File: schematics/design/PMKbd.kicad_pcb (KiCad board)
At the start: 2 copper layers, 28.1 x 39.6 mm, 92 parts, among them J1 Conn_01x01, J10 Conn_01x01, J11 Conn_01x01, J12 Conn_01x01, J13 Conn_01x01, J14 Conn_01x01, J15 Conn_01x01, J16 Conn_01x01, J17 Conn_01x01, J18 Conn_01x01, J19 Conn_01x01, J2 Conn_01x01, J20 Conn_01x01, J21 Conn_01x01, J22 Conn_01x01, J23 Conn_01x01, J24 Conn_01x01, J25 Conn_01x01, J26 Conn_01x01, J27 Conn_01x01, J28 Conn_01x01, J29 Conn_01x01, J3 Conn_01x01, J30 Conn_01x01, J31 Conn_01x01, J32 Conn_01x01, J33 Conn_01x01, J34 Conn_01x01, J35 Conn_01x01, J36 Conn_01x01, J37 Conn_01x01, J38 Conn_01x01, J39 Conn_01x01, J4 Conn_01x01, J40 Conn_01x01, J41 Conn_01x01, J42 Conn_01x01, J43 Conn_01x01, J44 Conn_01x01, J45 Conn_01x01, J46 Conn_01x01, J47 Conn_01x01, J48 Conn_01x01, J49 Conn_01x01, J5 Conn_01x01, J50 Conn_01x01, J51 Conn_01x01, J52 Conn_01x01, J53 Conn_01x01, J54 Conn_01x01, J55 Conn_01x01, J56 Conn_01x01, J57 Conn_01x01, J58 Conn_01x01, J59 Conn_01x01, J6 Conn_01x01, J60 Conn_01x01, J61 Conn_01x01, J62 Conn_01x01, J63 Conn_01x01, J64 Conn_01x01, J65 Conn_01x01, J66 Conn_01x01, J67 Conn_01x01, J68 Conn_01x01, J69 Conn_01x01, J7 Conn_01x01, J70 Conn_01x01, J71 Conn_01x01, J72 Conn_01x01, J73 Conn_01x01, J74 Conn_01x01, J8 Conn_01x01, J9 Conn_01x01, Q1 2N2222, Q2 2N2222, U1 Core51822_(B), U2 LT1117-3.3, U3 MCP73831-2-OT, U4 Core51822_(B)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

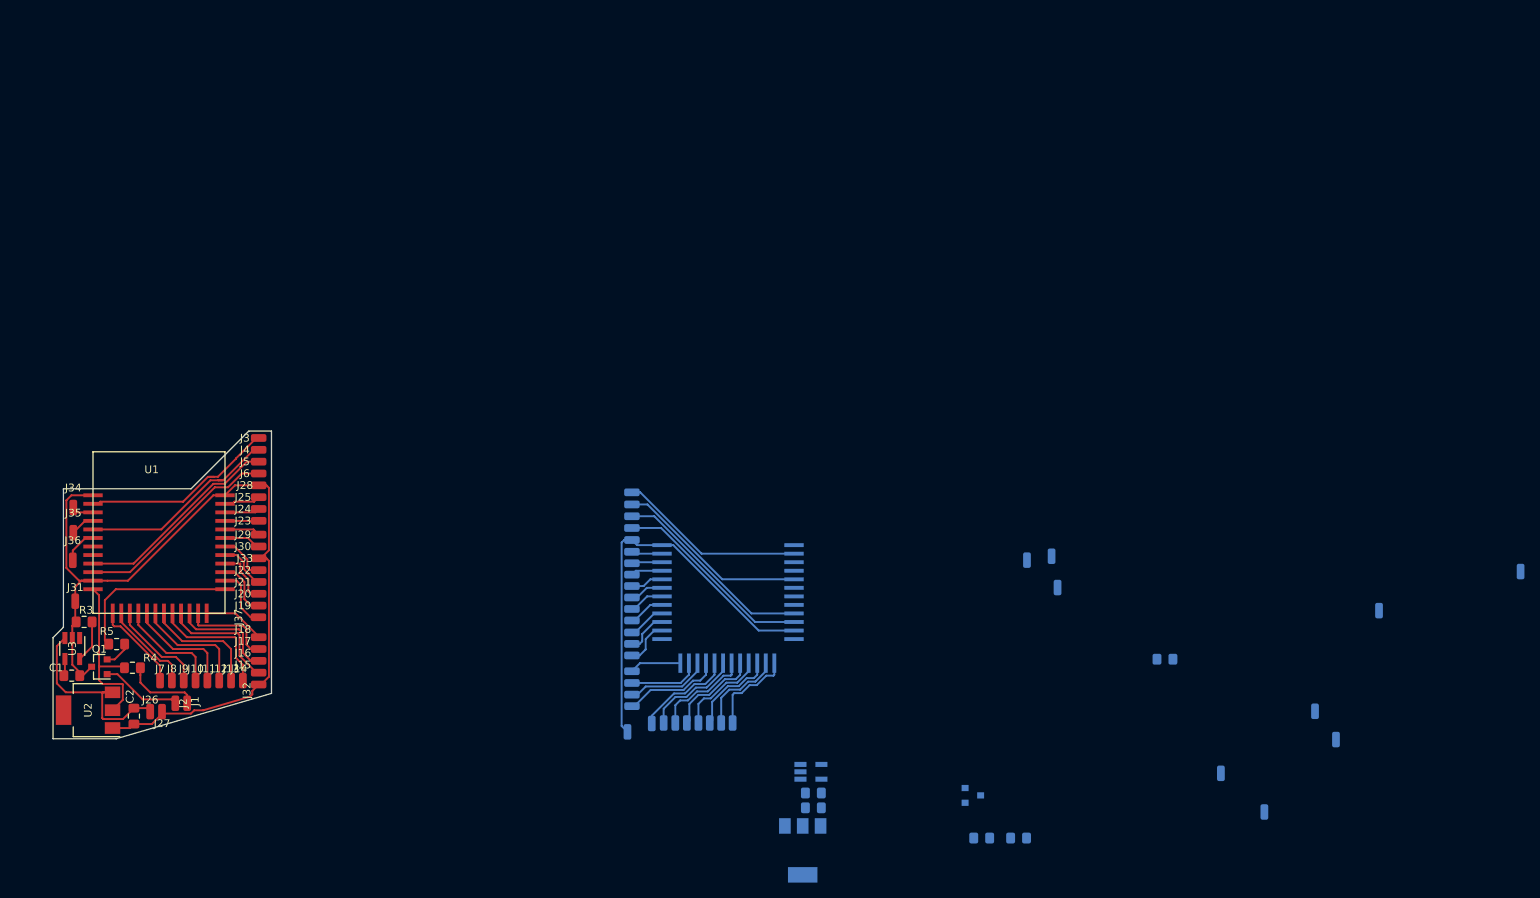
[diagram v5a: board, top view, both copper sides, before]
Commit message: first time right and left layouted
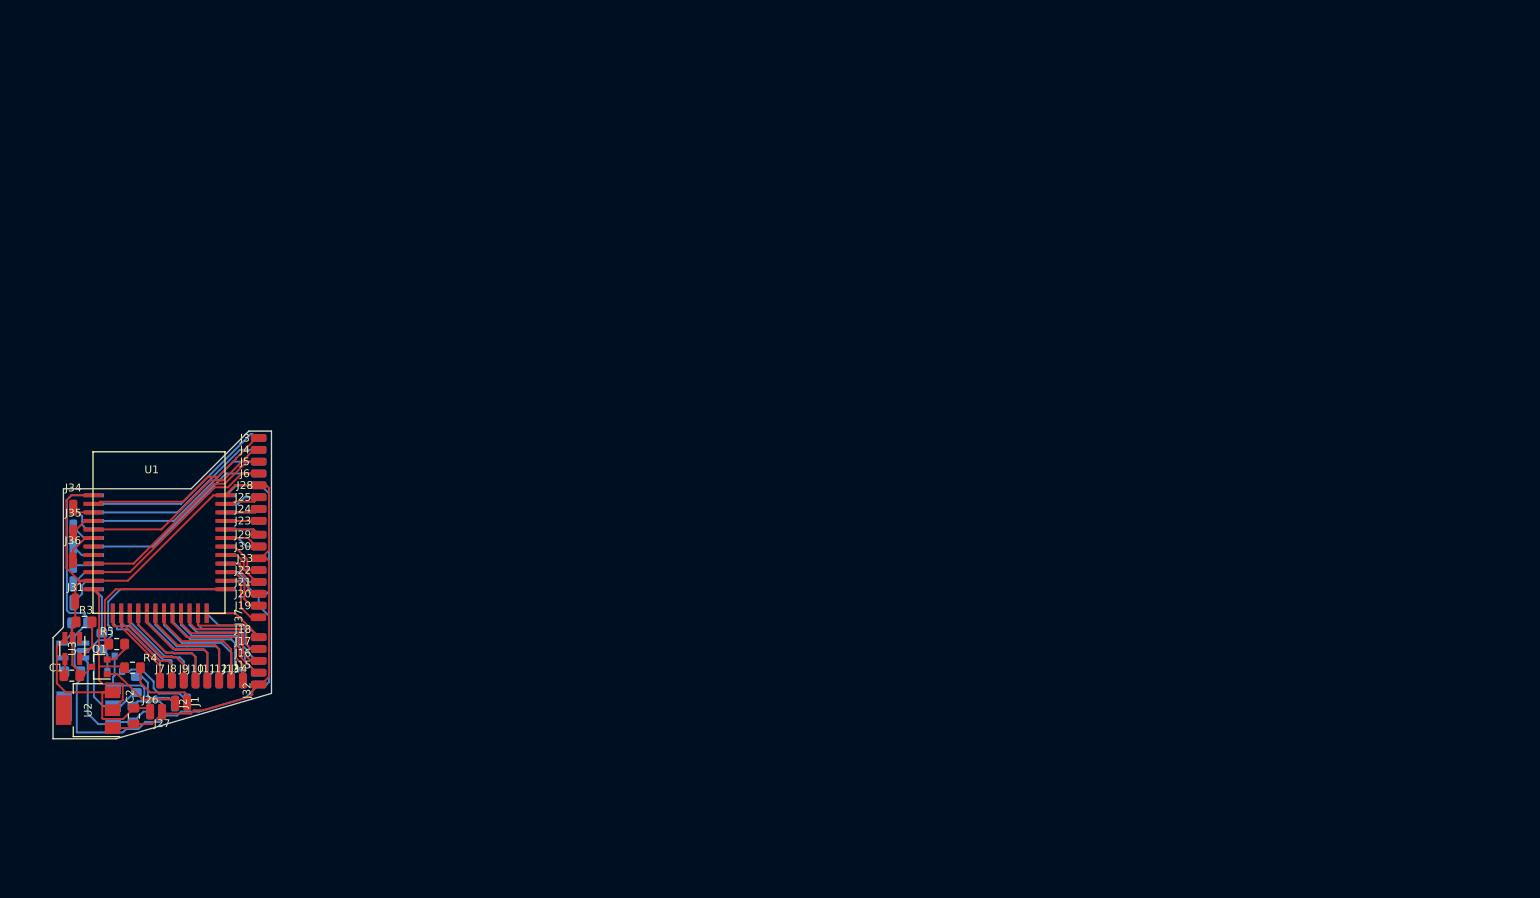
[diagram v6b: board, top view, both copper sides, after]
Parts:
- U5: footprint Package_TO_SOT_SMD:SOT-23-5_HandSoldering -> Package_TO_SOT_SMD:SOT-223
- U6: footprint Package_TO_SOT_SMD:SOT-223 -> Package_TO_SOT_SMD:SOT-23-5_HandSoldering
- moved J69 162.6 mm to (88.4, 84.8), turned to 90 degrees
- moved J63 152.8 mm to (74.4, 98.5)
- moved J64 148.5 mm to (75.9, 98.5)
- moved J65 144.3 mm to (88.4, 83.3), turned to 90 degrees
- moved J39 139.5 mm to (79.2, 97.2)
- moved R10 136.9 mm to (68.2, 89.4), turned to 270 degrees
- moved J38 135.0 mm to (77.6, 97.5)
- moved R8 124.1 mm to (65.3, 87.1), turned to 180 degrees
- moved Q2 111.8 mm to (69.8, 92.3), turned to 90 degrees
- moved R9 110.6 mm to (72.6, 95.0), turned to 270 degrees
- moved J73 103.0 mm to (88.4, 77.2), turned to 90 degrees
- moved J71 102.3 mm to (88.4, 72.4), turned to 90 degrees
- moved J72 99.1 mm to (88.4, 73.9), turned to 90 degrees
- moved U6 97.5 mm to (64.5, 90.6), turned to 180 degrees
- moved C3 96.6 mm to (64.5, 93.3), turned to 0 degrees
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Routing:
- net GND_R: track 51.9 -> 119.6 mm
- net 3.3V_R: track 0.00 -> 36.6 mm
- net S26: track 26.1 -> 4.51 mm
- net S27: track 25.9 -> 4.68 mm
- net S46: track 3.98 -> 25.1 mm
- net S45: track 3.93 -> 24.5 mm
- net S43: track 4.55 -> 25.1 mm
- net S25: track 24.9 -> 4.44 mm
- net S44: track 4.08 -> 24.3 mm
- net S24: track 24.1 -> 4.52 mm
- net Net-(BT2-Pad1): track 0.00 -> 16.7 mm
- net Net-(J39-Pad1): track 0.00 -> 10.7 mm
- net Net-(J38-Pad1): track 0.00 -> 7.79 mm
- net LED_R: track 0.00 -> 6.06 mm
- net S39: track 6.67 -> 12.0 mm
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
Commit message: minimal improvements
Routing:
- net Net-(J39-Pad1): track 10.7 -> 12.5 mm
- net GND_R: track 119.6 -> 121.3 mm
- net 3.3V_R: track 36.6 -> 38.0 mm
- net S38: track 12.5 -> 11.4 mm
- net S36: track 13.6 -> 12.8 mm
- net S39: track 12.0 -> 11.2 mm
- net Net-(J38-Pad1): track 7.79 -> 7.15 mm
- net S37: track 12.6 -> 13.2 mm
